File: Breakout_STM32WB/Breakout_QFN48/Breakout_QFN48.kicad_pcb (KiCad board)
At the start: 4 copper layers, 24 x 33.8 mm, 80 parts, among them J1 Debug conn, J10 Conn_01x01, J11 Conn_01x01, J12 Conn_01x01, J13 Conn_01x01, J14 Conn_01x01, J15 Conn_01x01, J16 Conn_01x01, J17 Conn_01x01, J18 Conn_01x01, J19 Conn_01x01, J2 Conn_01x01, J20 Conn_01x01, J21 Conn_01x01, J22 Conn_01x01, J23 Conn_01x01, J24 Conn_01x01, J25 Conn_01x01, J26 Conn_01x01, J27 Conn_01x01, J28 Conn_01x01, J3 Conn_01x01, J30 Conn_01x01, J31 Conn_01x01, J32 Conn_01x01, J33 Conn_01x01, J34 Conn_01x01, J35 Conn_01x01, J36 Conn_01x01, J37 Conn_01x01, J38 Conn_01x01, J39 Conn_01x01, J4 Conn_01x01, J40 Conn_01x01, J41 Conn_01x01, J42 Conn_01x01, J43 Conn_01x01, J44 Conn_01x01, J45 Conn_01x01, J46 Conn_01x01, J47 Conn_01x01, J48 Conn_01x01, J5 Conn_01x01, J6 Conn_01x01, J7 Conn_01x01, J8 Conn_01x01, J9 Conn_01x01, U1 STM32WB55Cx, U2 LFL212G45TC1A007, U3 MCP1700-3302E_SOT23, Y1 NX2012SA_32-768kHz, Y2 NX2016_32M

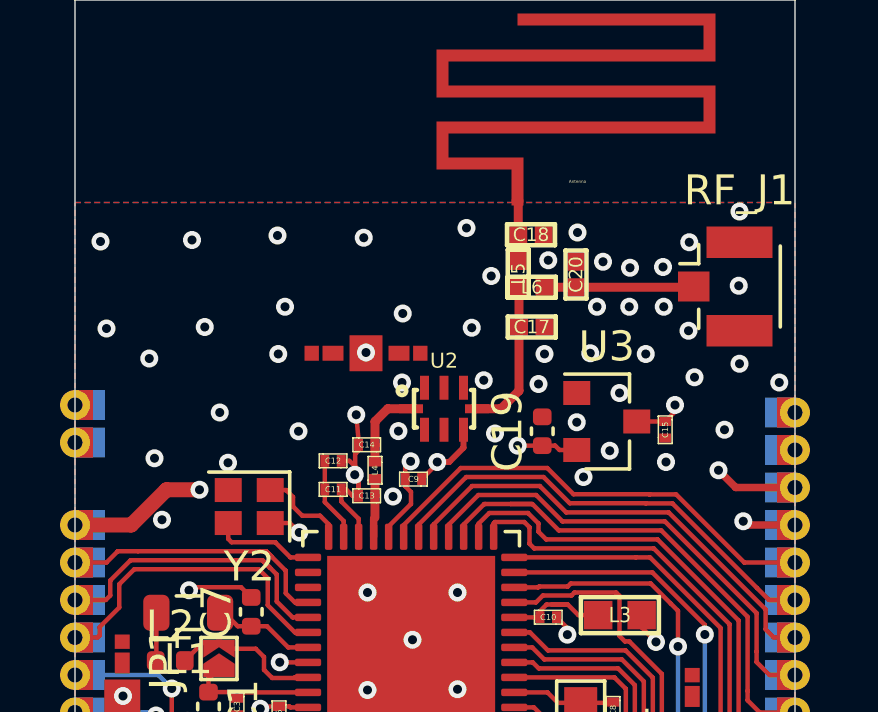
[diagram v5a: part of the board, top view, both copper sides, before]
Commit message: Breakout_STM32WB : update layout
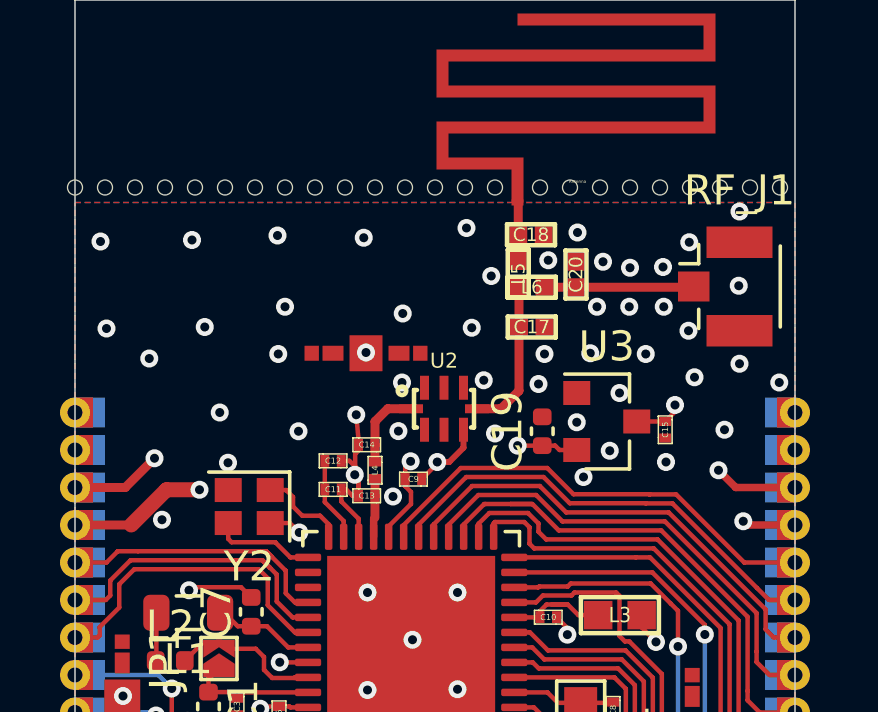
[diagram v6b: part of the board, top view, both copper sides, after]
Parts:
- added Hole_0.5mm: VAL**, Yame_library:Hole_0.5mm, F.Cu at (128.5, 85.2)
- added Hole_0.5mm: VAL**, Yame_library:Hole_0.5mm, F.Cu at (105.0, 85.2)
- added Hole_0.5mm: VAL**, Yame_library:Hole_0.5mm, F.Cu at (106.0, 85.2)
- added Hole_0.5mm: VAL**, Yame_library:Hole_0.5mm, F.Cu at (107.0, 85.2)
- added Hole_0.5mm: VAL**, Yame_library:Hole_0.5mm, F.Cu at (108.0, 85.2)
- added Hole_0.5mm: VAL**, Yame_library:Hole_0.5mm, F.Cu at (109.0, 85.2)
- added Hole_0.5mm: VAL**, Yame_library:Hole_0.5mm, F.Cu at (110.0, 85.2)
- added Hole_0.5mm: VAL**, Yame_library:Hole_0.5mm, F.Cu at (111.0, 85.2)
- added Hole_0.5mm: VAL**, Yame_library:Hole_0.5mm, F.Cu at (112.0, 85.2)
- added Hole_0.5mm: VAL**, Yame_library:Hole_0.5mm, F.Cu at (113.0, 85.2)
- added Hole_0.5mm: VAL**, Yame_library:Hole_0.5mm, F.Cu at (114.0, 85.2)
- added Hole_0.5mm: VAL**, Yame_library:Hole_0.5mm, F.Cu at (127.5, 85.2)
- added Hole_0.5mm: VAL**, Yame_library:Hole_0.5mm, F.Cu at (115.0, 85.2)
- added Hole_0.5mm: VAL**, Yame_library:Hole_0.5mm, F.Cu at (116.0, 85.2)
- added Hole_0.5mm: VAL**, Yame_library:Hole_0.5mm, F.Cu at (117.0, 85.2)
- added Hole_0.5mm: VAL**, Yame_library:Hole_0.5mm, F.Cu at (118.0, 85.2)
- added Hole_0.5mm: VAL**, Yame_library:Hole_0.5mm, F.Cu at (119.0, 85.2)
- added Hole_0.5mm: VAL**, Yame_library:Hole_0.5mm, F.Cu at (126.5, 85.2)
- added Hole_0.5mm: VAL**, Yame_library:Hole_0.5mm, F.Cu at (125.5, 85.2)
- added Hole_0.5mm: VAL**, Yame_library:Hole_0.5mm, F.Cu at (124.5, 85.2)
- added Hole_0.5mm: VAL**, Yame_library:Hole_0.5mm, F.Cu at (123.5, 85.2)
- added Hole_0.5mm: VAL**, Yame_library:Hole_0.5mm, F.Cu at (122.5, 85.2)
- added Hole_0.5mm: VAL**, Yame_library:Hole_0.5mm, F.Cu at (121.5, 85.2)
- added Hole_0.5mm: VAL**, Yame_library:Hole_0.5mm, F.Cu at (120.5, 85.2)
- added J29: Conn_01x01, Yame_library:Castellated, F.Cu at (105.0, 95.2)
- moved J36 0.25 mm to (105.0, 94.0)
- moved J38 0.25 mm to (105.0, 92.8)
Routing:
- net GND: track 53.5 -> 56.2 mm

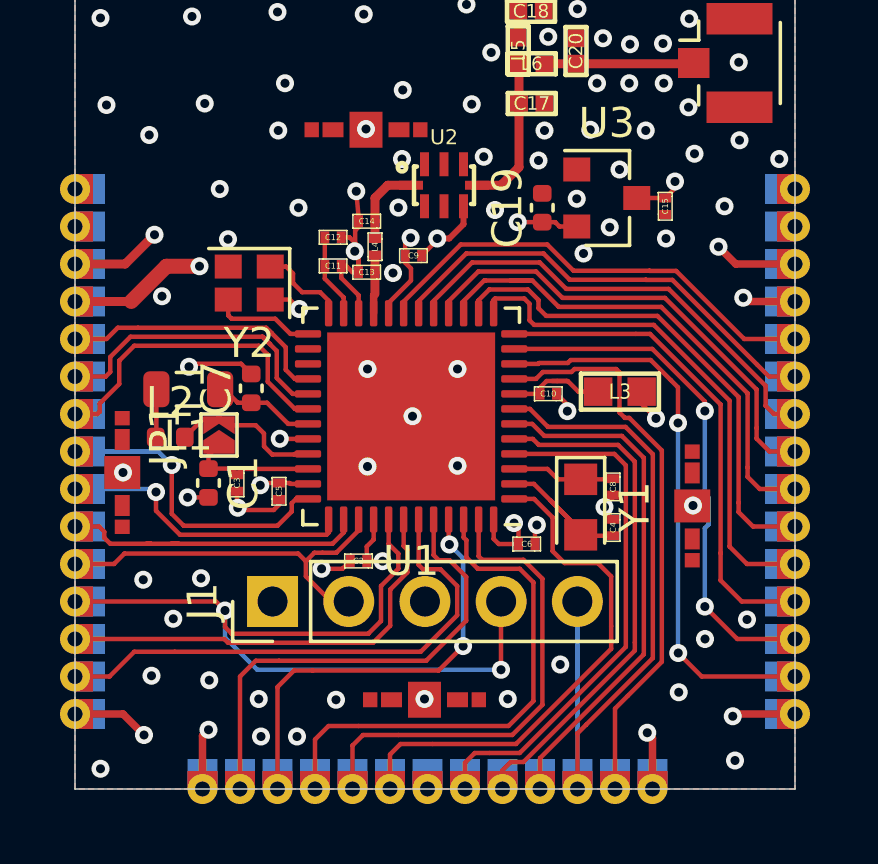
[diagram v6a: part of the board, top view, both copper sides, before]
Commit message: update castellated holes minimum diameter
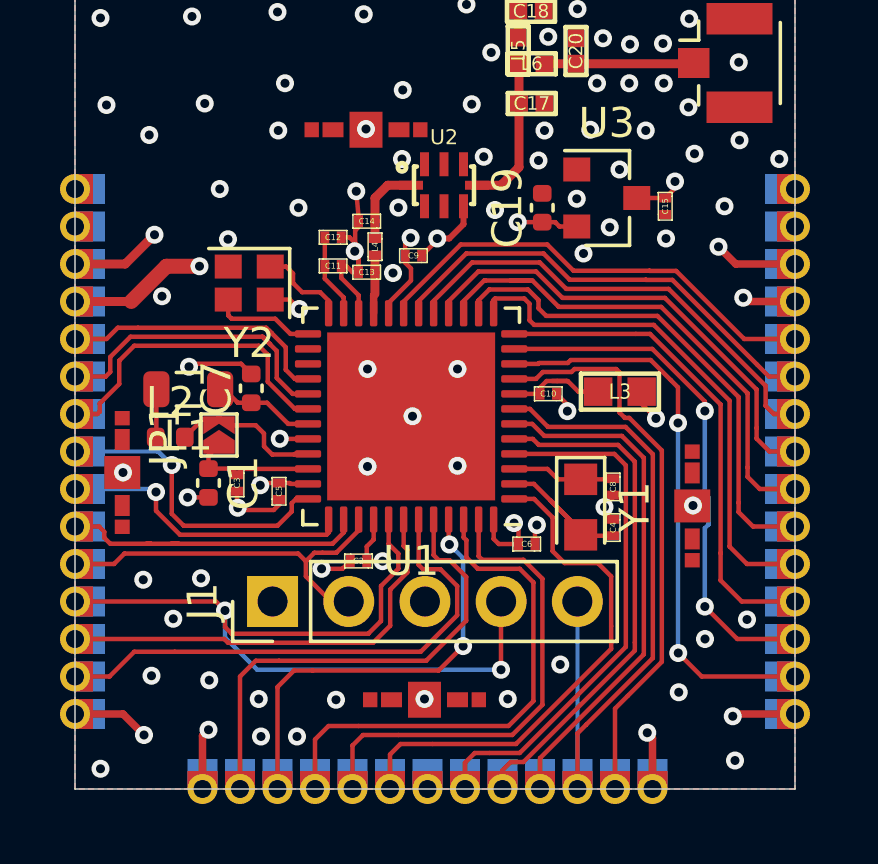
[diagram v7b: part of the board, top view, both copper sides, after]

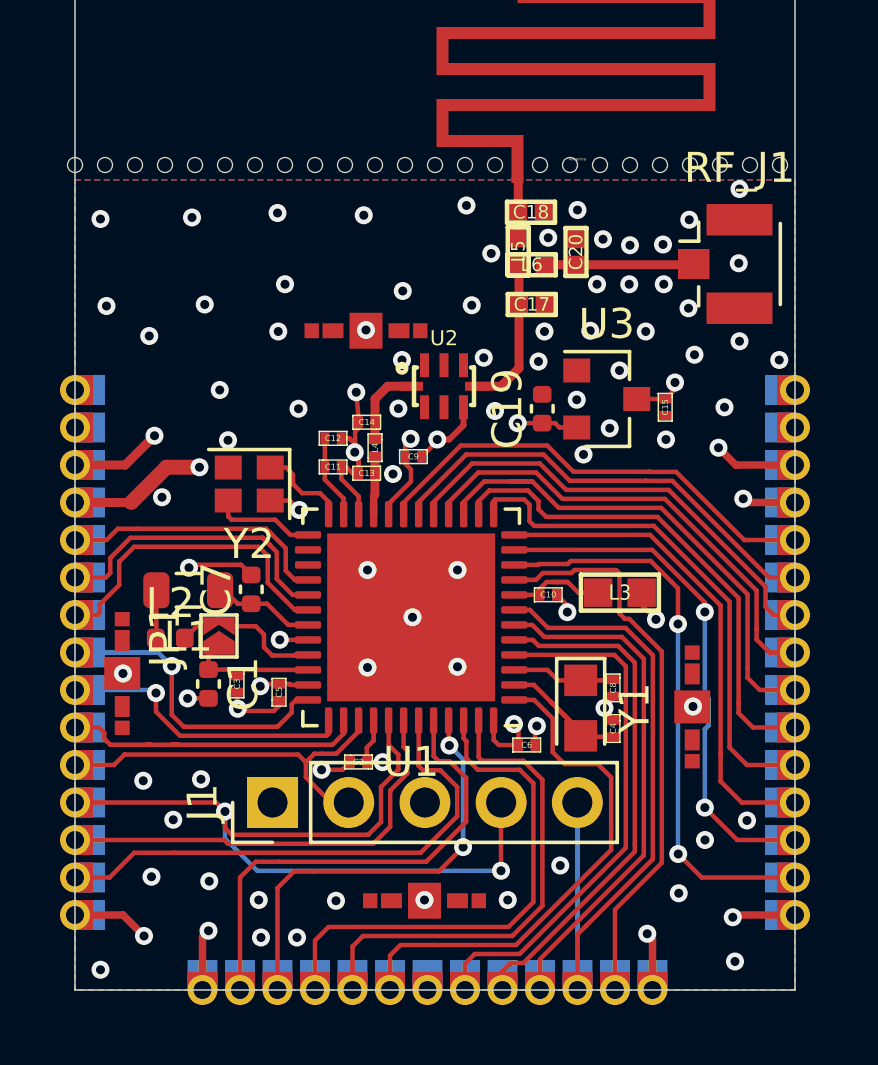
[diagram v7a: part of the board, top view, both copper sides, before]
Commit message: Update following Mr Granier remarks
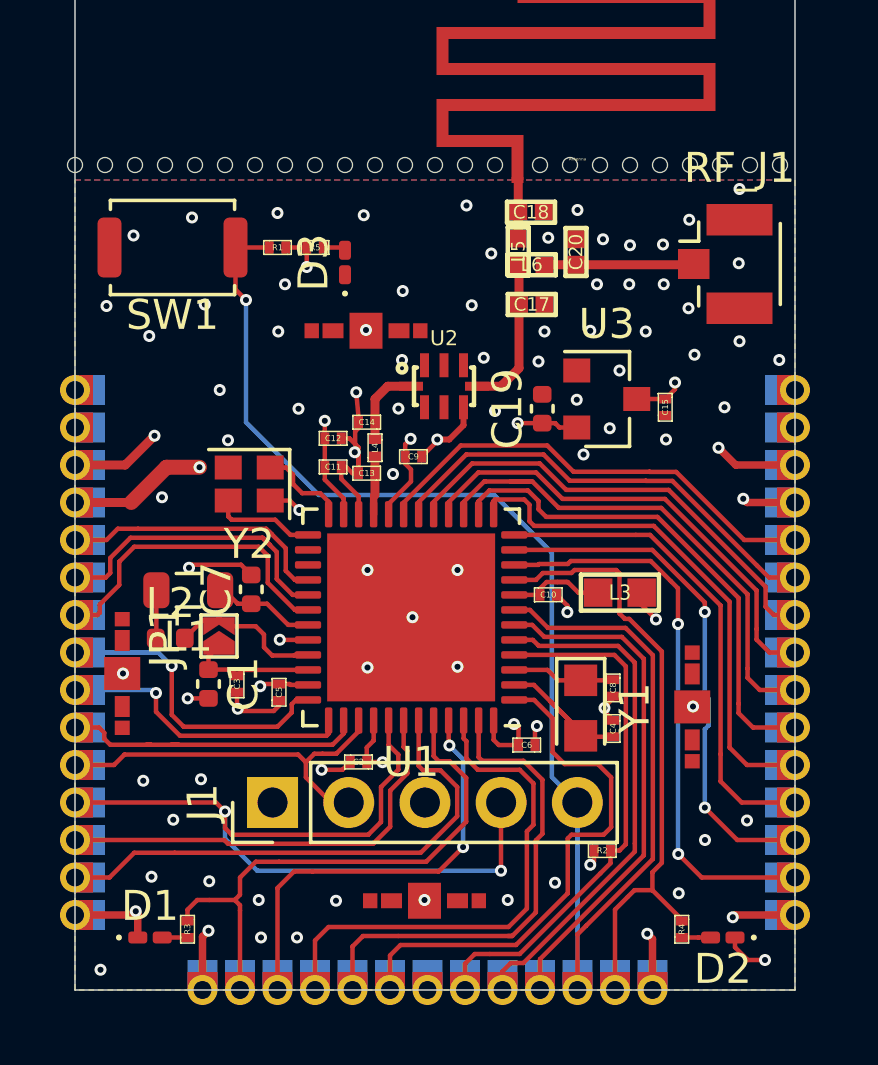
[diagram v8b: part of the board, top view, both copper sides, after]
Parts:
- added D1: IN-S21AT2B, LED_SMD:LED_0201_0603Metric_Pad0.64x0.40mm_HandSolder, F.Cu at (107.5, 111.0)
- added D2: IN-S21AT2B, LED_SMD:LED_0201_0603Metric_Pad0.64x0.40mm_HandSolder, F.Cu at (126.6, 111.0)
- added D3: IN-S21AT2B, LED_SMD:LED_0201_0603Metric_Pad0.64x0.40mm_HandSolder, F.Cu at (114.0, 88.5)
- added R1: 100k, Yame_library:SM0201-MR, F.Cu at (111.8, 88.0)
- added R2: 100k, Yame_library:SM0201-MR, F.Cu at (122.6, 108.1)
- added R3: 1k, Yame_library:SM0201-MR, F.Cu at (108.8, 110.7)
- added R4: 1k, Yame_library:SM0201-MR, F.Cu at (125.2, 110.7)
- added R5: 1k, Yame_library:SM0201-MR, F.Cu at (113.0, 88.0)
- added SW1: Reset, Button_Switch_SMD:SW_Push_SPST_NO_Alps_SKRK, F.Cu at (108.2, 88.0)
- C13: value 100n -> 0.8pF
- C14: value 100n -> 0.3pF
- C17, C18, C20: value 100n -> C
- L3: value Ferrite beads 0603 -> BK1608TS601-T
- L4: value L -> 2.7nH
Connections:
- net Net-(J22-Pad1) renamed /LED1
- net Net-(J3-Pad1) renamed /BOOT0
- net Net-(J4-Pad1) renamed /LED2
- C11 pad 1: Net-(C11-Pad1) -> +3V3
- C12 pad 1: Net-(C11-Pad1) -> +3V3
- U1 pad 23: Net-(C11-Pad1) -> +3V3
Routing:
- net /NRST: track 23.5 -> 51.3 mm, vias 0 -> 1
- net +3V3: track 30.7 -> 36.0 mm, vias 7 -> 10
- net Net-(C11-Pad1): track 2.79 -> 0.00 mm
- net /LED1: track 16.1 -> 18.3 mm
- net GND: track 56.2 -> 58.1 mm
- net /LED2: track 18.9 -> 20.7 mm
- net Net-(D2-Pad2): track 0.00 -> 1.01 mm
- net Net-(D1-Pad2): track 0.00 -> 0.84 mm
- net Net-(D3-Pad2): track 0.00 -> 0.76 mm
- net Net-(J2-Pad1): track 17.1 -> 17.7 mm
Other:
- rule via_min_size: 0.6 -> 0.4
